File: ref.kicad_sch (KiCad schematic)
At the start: 44 parts, among them Q1 Q_NPN_BCE, U4 ADR1000, U5 Opamp_Dual, U8 ADA4523-1

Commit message: asdf
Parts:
- added JP14, JP15, JP16, JP17, JP18, JP19: Jumper_2_Open, Jumper:SolderJumper-2_P1.3mm_Open_RoundedPad1.0x1.5mm, symbol Jumper:Jumper_2_Open
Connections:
- net ADR_Pin4: now also RN1.12 (R3.2), JP17.2 (B); no longer RN1.3 (R3.1)
- net ADR_Pin5: now also JP16.2 (B)
- net ADR_Pin6: now also JP14.2 (B)
- net ADR_Pin8: now also JP15.2 (B)
- net RN1_Pin1: now also JP16.1 (A)
- net RN1_Pin12: now also RN1.3 (R3.1), JP17.1 (A); no longer RN1.12 (R3.2)
- net RN1_Pin2: now also JP15.1 (A)
- net RN1_Pin5: now also JP14.1 (A)
- net RN1_Pin6: now also JP19.1 (A)
- net RN1_Pin7: now also JP18.2 (B)
- net U8_Pin2: now also JP18.1 (A), JP19.2 (B)
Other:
- moved on the sheet: RN1C, RN1E, RN1F, RN1G

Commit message: flood of prototyping area
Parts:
- added JP20: Jumper_2_Bridged, Jumper:SolderJumper-2_P1.3mm_Bridged_RoundedPad1.0x1.5mm, symbol Jumper:Jumper_2_Bridged
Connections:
- net DC_DC_GND: now also JP20.2 (B)
- new net shield_maybe: JP20.1 (A)
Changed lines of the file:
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@@
   (junction (at 153.67 52.07) (diameter 0) (color 0 0 0 0)
   )
+  (junction (at 62.23 130.81) (diameter 0) (color 0 0 0 0)
+  )
   (junction (at 140.97 52.07) (diameter 0) (color 0 0 0 0)
   )
@@
     (stroke (width 0) (type default) (color 0 0 0 0))
   )
+  (wire (pts (xy 45.72 130.81) (xy 49.53 130.81))
+    (stroke (width 0) (type default) (color 0 0 0 0))
+  )
   (wire (pts (xy 191.77 78.74) (xy 189.23 78.74))
     (stroke (width 0) (type default) (color 0 0 0 0))
@@
   )
   (wire (pts (xy 144.78 78.74) (xy 144.78 77.47))
+    (stroke (width 0) (type default) (color 0 0 0 0))
+  )
+  (wire (pts (xy 59.69 130.81) (xy 62.23 130.81))
     (stroke (width 0) (type default) (color 0 0 0 0))
   )
@@
   )
   (label "ADR_Pin7" (at 138.43 102.87 180)
+    (effects (font (size 0.5 0.5)) (justify right bottom))
+  )
+  (label "shield_maybe" (at 45.72 130.81 180)
     (effects (font (size 0.5 0.5)) (justify right bottom))
   )
@@
       (effects (font (size 1.27 1.27)) hide)
     )
+    (pin "1")
+    (pin "2")
+  )
+  (symbol (lib_id "Jumper:Jumper_2_Bridged") (at 54.61 130.81 0) (unit 1)
+    (in_bom yes) (on_board yes) (fields_autoplaced)
+    (property "Reference" "JP20" (id 0) (at 54.61 127 0))
+    (property "Value" "Jumper_2_Bridged" (id 1) (at 54.61 127 0)
+      (effects (font (size 1.27 1.27)) hide)
+    )
+    (property "Footprint" "Jumper:SolderJumper-2_P1.3mm_Bridged_RoundedPad1.0x1.5mm" (id 2) (at 54.61 130.81 0)
+      (effects (font (size 1.27 1.27)) hide)
+    )
+    (property "Datasheet" "~" (id 3) (at 54.61 130.81 0)
+      (effects (font (size 1.27 1.27)) hide)
+    )

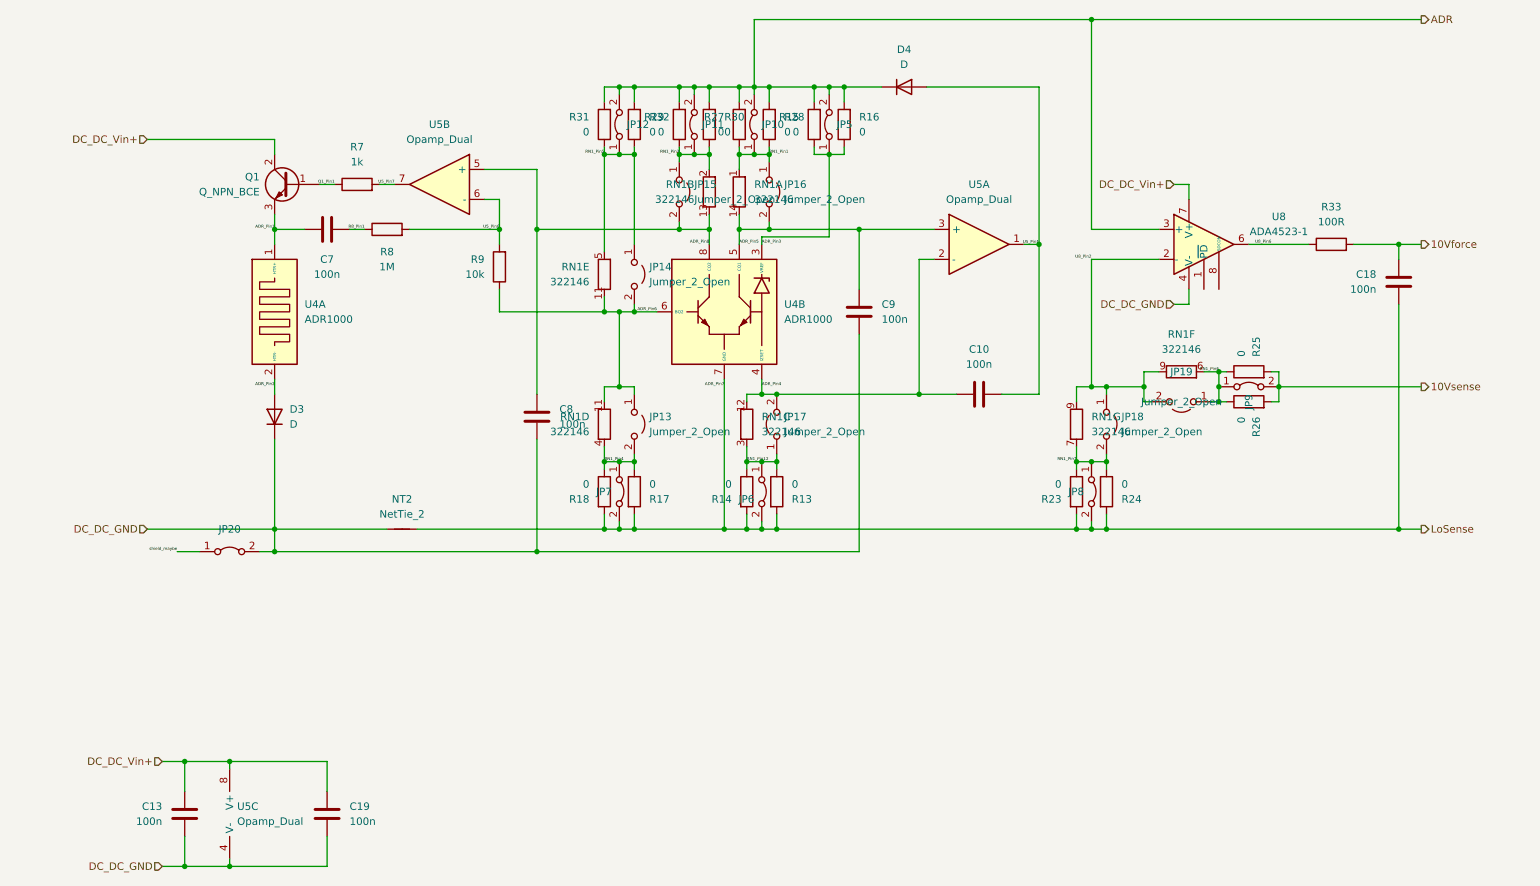
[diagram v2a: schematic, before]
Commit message: reference designators reassigned
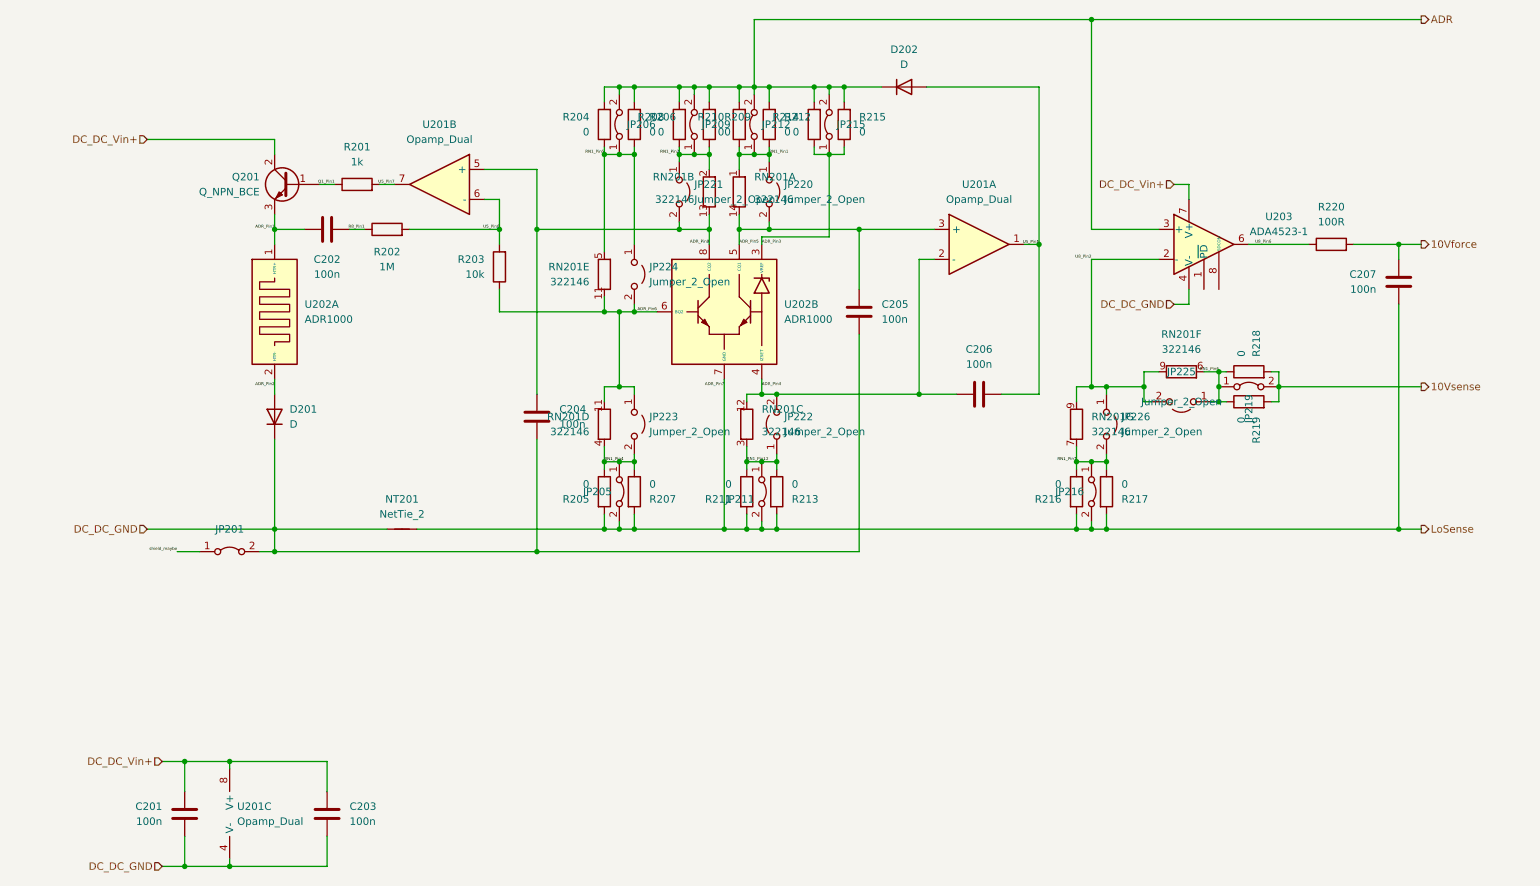
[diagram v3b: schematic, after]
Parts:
- renumbered C13 to C201, C7 to C202, C19 to C203, C8 to C204, C9 to C205, C10 to C206, C18 to C207, D3 to D201, D4 to D202, JP20 to JP201, JP7 to JP205, JP12 to JP206, JP11 to JP209, JP6 to JP211, JP10 to JP212, JP5 to JP215, JP8 to JP216, JP9 to JP219, JP16 to JP220, JP15 to JP221, JP17 to JP222, JP13 to JP223, JP14 to JP224, JP19 to JP225, JP18 to JP226, NT2 to NT201, Q1 to Q201, R7 to R201, R8 to R202, R9 to R203, R31 to R204, R18 to R205, R32 to R206, R17 to R207, R29 to R208, R30 to R209, R27 to R210, R14 to R211, R28 to R212, R13 to R213, R15 to R214, R16 to R215, R23 to R216, R24 to R217, R25 to R218, R26 to R219, R33 to R220, RN1 to RN201, U5 to U201, U4 to U202, U8 to U203

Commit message: generated bom, pdf, gerbers
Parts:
- NT201: now left out of the parts list
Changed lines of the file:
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@@
   )
   (symbol (lib_id "Device:NetTie_2") (at 83.82 127 0) (unit 1)
-    (in_bom yes) (on_board yes) (fields_autoplaced)
+    (in_bom no) (on_board yes) (fields_autoplaced)
     (property "Reference" "NT201" (id 0) (at 83.82 121.92 0))
     (property "Value" "NetTie_2" (id 1) (at 83.82 124.46 0))

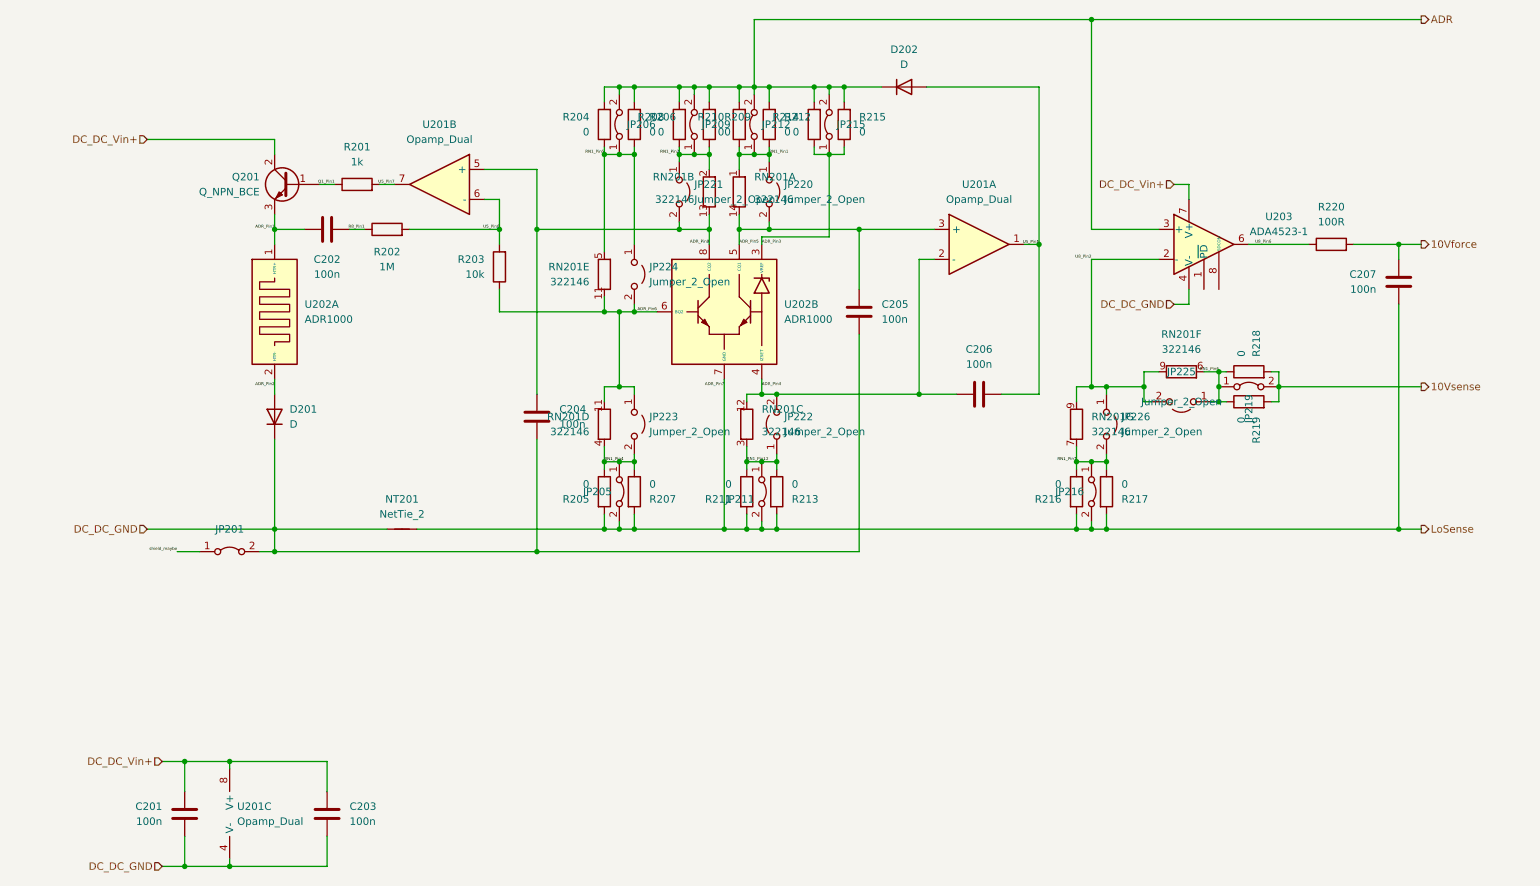
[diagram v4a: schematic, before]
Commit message: Obligatory bugs in the first production run:
- Missing stability cap between buffer out and -in
- Missing cap for autozeroing buffer
- Side status LEDs need to be flipped
- Many schematic net names wrong
- LDO power good implemented wrong
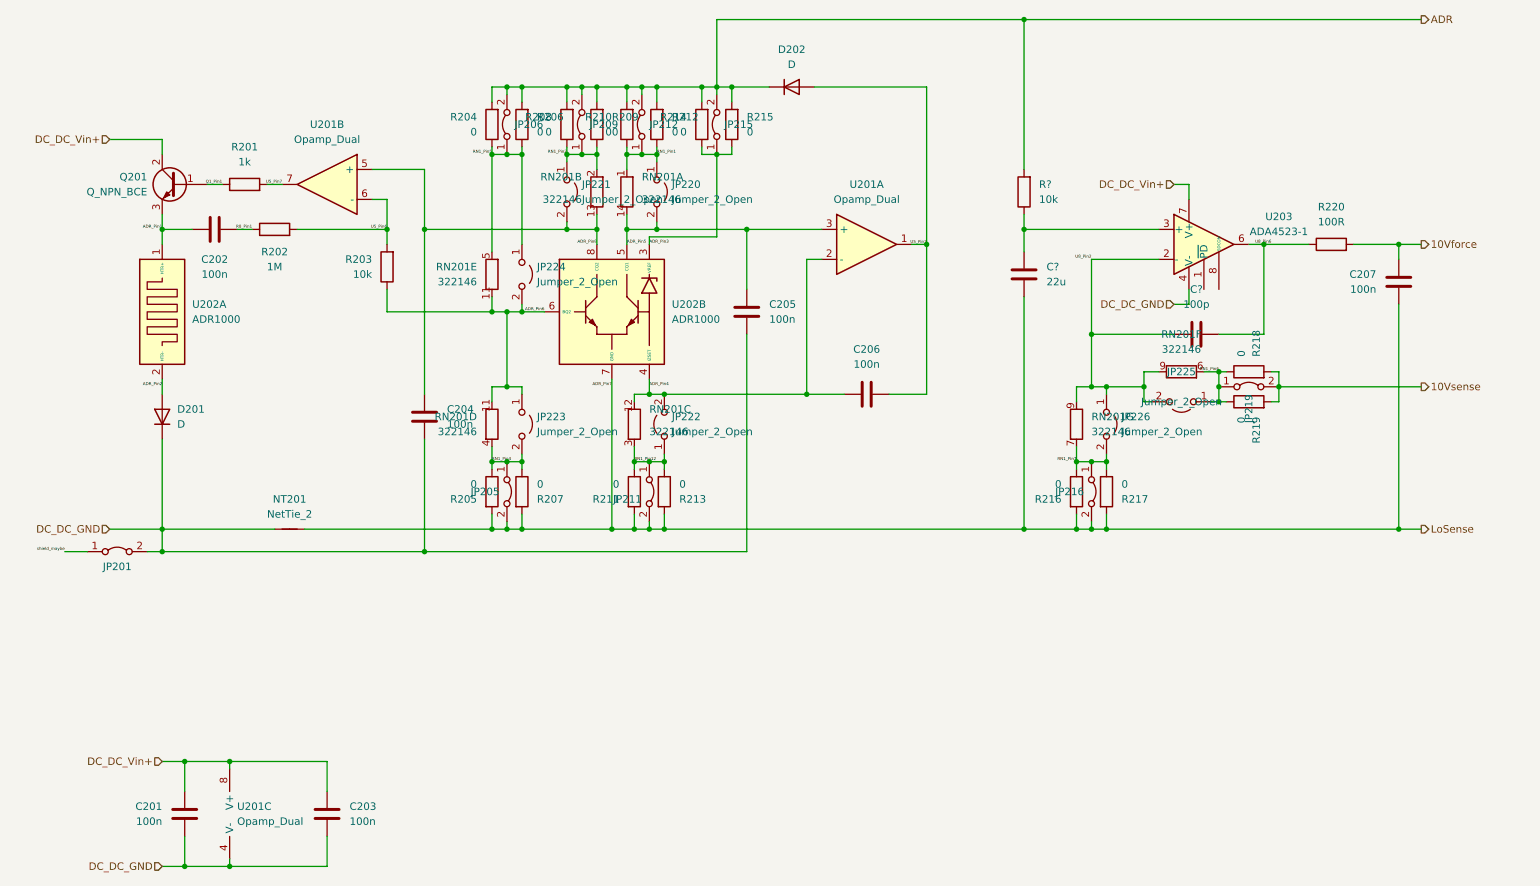
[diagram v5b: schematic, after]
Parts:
- added C?: 22u, Capacitor_SMD:C_1206_3216Metric, symbol Device:C
- added C?: 100p, Capacitor_SMD:C_0805_2012Metric, symbol Device:C
- added R?: 10k, Resistor_SMD:R_0805_2012Metric, symbol Device:R
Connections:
- net ADR: now also R?.2; no longer U203.3 (+)
- net LoSense: now also C?.2
- net U8_Pin2: now also C?.2
- net U8_Pin6: now also C?.1
- new net: C?.1, R?.1, U203.3 (+)
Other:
- moved on the sheet: C202, C204, C205, C206, D201, D202, JP201, JP205, JP206, JP209, JP211, JP212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

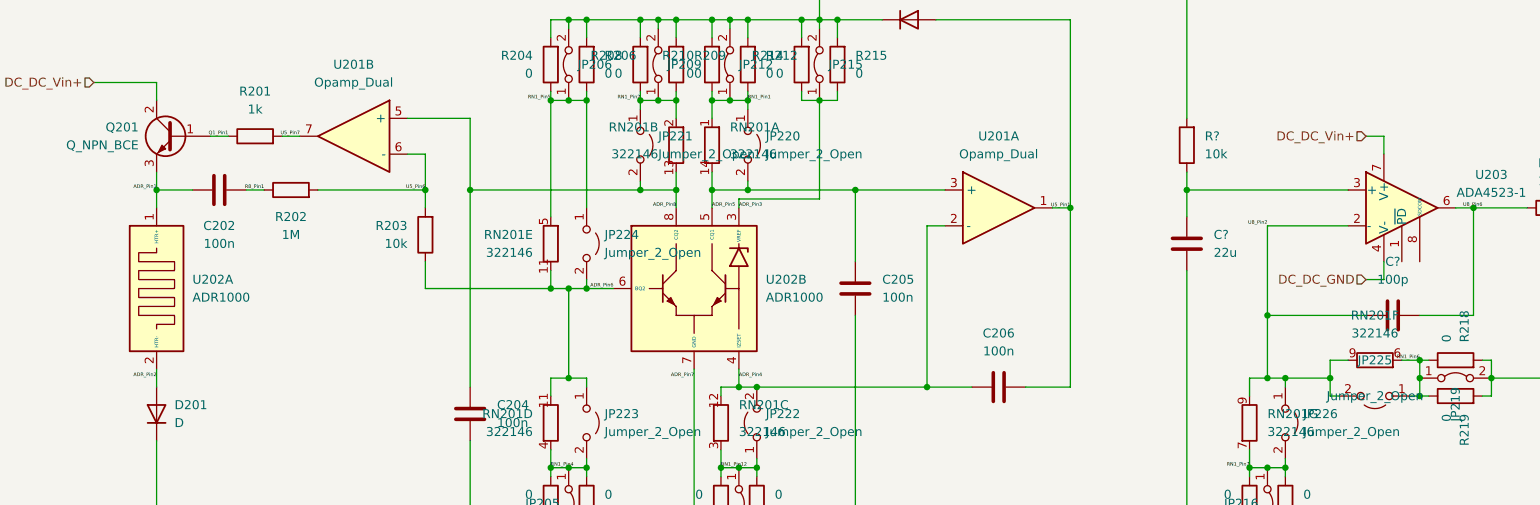
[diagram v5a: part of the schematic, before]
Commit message: GNDf terminal was sharing a via with heater return
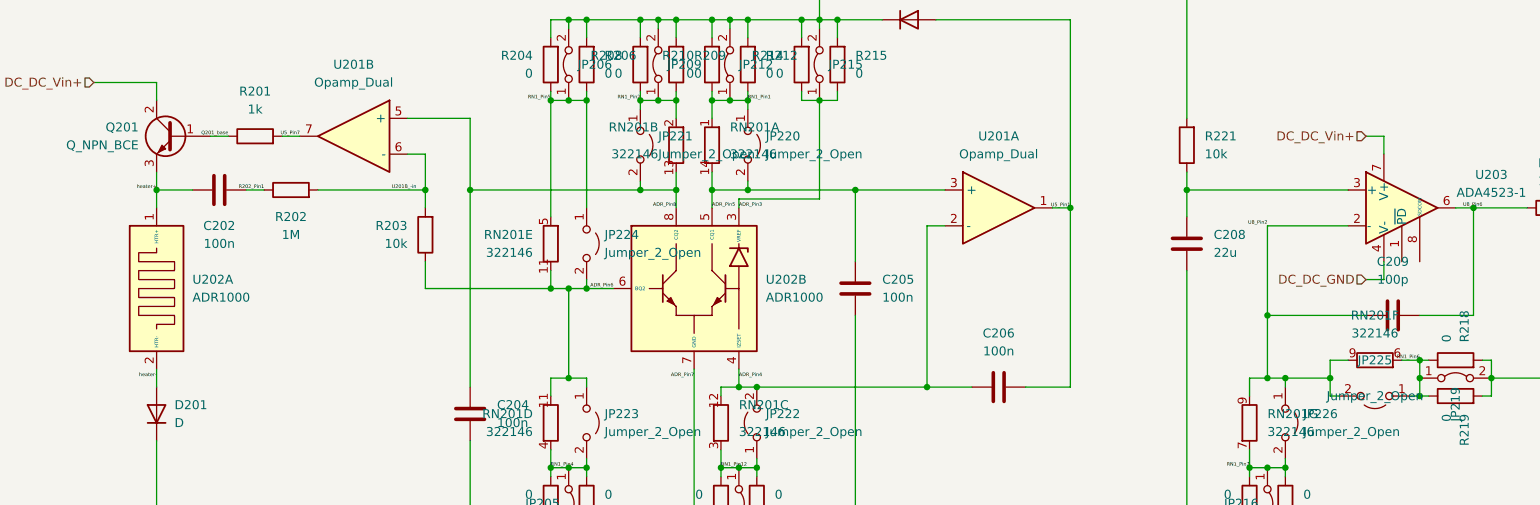
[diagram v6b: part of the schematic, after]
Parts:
- gave numbers to parts that had none: 3
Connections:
- net ADR_Pin1 renamed heater+
- net ADR_Pin2 renamed heater-
- net Q1_Pin1 renamed Q201_base
- net R8_Pin1 renamed R202_Pin1
- net U5_Pin6 renamed U201B_-in
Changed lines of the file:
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@@
     (effects (font (size 0.5 0.5)) (justify right bottom))
   )
-  (label "U5_Pin6" (at 81.28 76.2 180)
-    (effects (font (size 0.5 0.5)) (justify right bottom))
-  )
-  (label "R8_Pin1" (at 58.42 76.2 180)
-    (effects (font (size 0.5 0.5)) (justify right bottom))
-  )
-  (label "ADR_Pin2" (at 43.18 102.87 180)
+  (label "U201B_-in" (at 80.01 76.2 180)
+    (effects (font (size 0.5 0.5)) (justify right bottom))
+  )
+  (label "R202_Pin1" (at 58.42 76.2 180)
+    (effects (font (size 0.5 0.5)) (justify right bottom))
+  )
+  (label "heater-" (at 43.18 102.87 180)
     (effects (font (size 0.5 0.5)) (justify right bottom))
   )
@@
     (effects (font (size 0.5 0.5)) (justify right bottom))
   )
-  (label "Q1_Pin1" (at 53.34 68.58 180)
+  (label "Q201_base" (at 53.34 68.58 180)
     (effects (font (size 0.5 0.5)) (justify right bottom))
   )
@@
     (effects (font (size 0.5 0.5)) (justify left bottom))
   )
-  (label "ADR_Pin1" (at 43.18 76.2 180)
+  (label "heater+" (at 43.18 76.2 180)
     (effects (font (size 0.5 0.5)) (justify right bottom))
   )
@@
   (symbol (lib_id "Device:C") (at 189.23 83.82 0) (unit 1)
     (in_bom yes) (on_board yes) (fields_autoplaced)
-    (property "Reference" "C?" (id 0) (at 193.04 82.5499 0)
+    (property "Reference" "C208" (id 0) (at 193.04 82.5499 0)
       (effects (font (size 1.27 1.27)) (justify left))
     )
@@
   (symbol (lib_id "Device:C") (at 218.44 93.98 270) (unit 1)
     (in_bom yes) (on_board yes) (fields_autoplaced)
-    (property "Reference" "C?" (id 0) (at 218.44 86.36 90))
+    (property "Reference" "C209" (id 0) (at 218.44 86.36 90))
     (property "Value" "100p" (id 1) (at 218.44 88.9 90))
     (property "Footprint" "Capacitor_SMD:C_0805_2012Metric" (id 2) (at 214.63 94.9452 0)
@@
   (symbol (lib_id "Device:R") (at 189.23 69.85 180) (unit 1)
     (in_bom yes) (on_board yes) (fields_autoplaced)
-    (property "Reference" "R?" (id 0) (at 191.77 68.5799 0)
-      (effects (font (size 1.27 1.27)) (justify right))
-    )
+    (property "Reference" "R221" (id 0) (at 191.77 68.5799 0)
+      (effects (font (size 1.27 1.27)) (justify right))
+    )
